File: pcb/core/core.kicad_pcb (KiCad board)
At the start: 2 copper layers, 24 x 26 mm, 25 parts, among them J1 Conn_01x10, J2 Conn_01x07, J3 Conn_ARM_SWD_TagConnect_TC203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, J4 Conn_01x10, U1 bq25185, U2 MDBT50-512K, U3 MCP1662-xOT

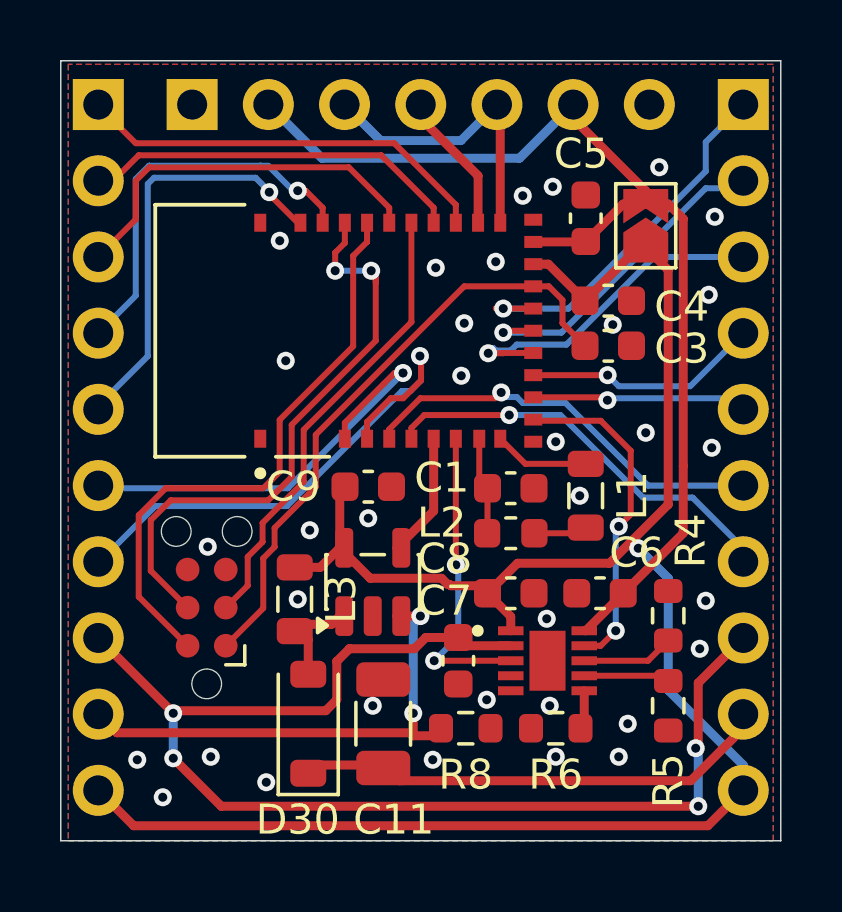
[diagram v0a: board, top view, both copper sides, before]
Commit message: Some fixes on PCB
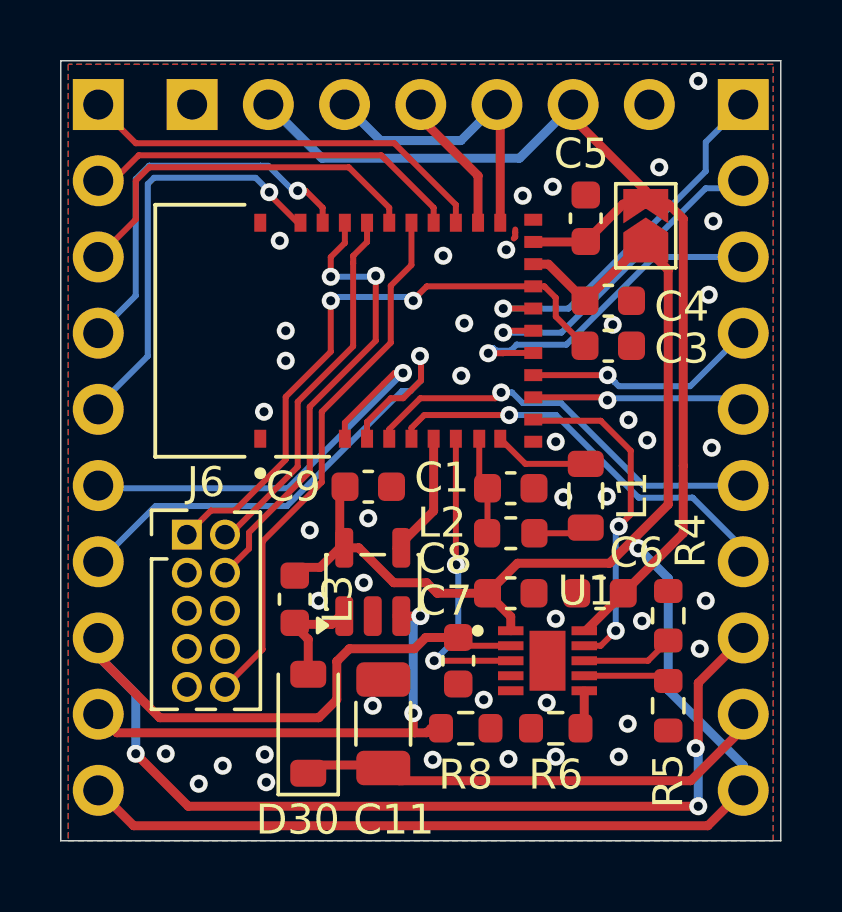
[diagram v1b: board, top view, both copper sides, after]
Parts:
- removed J3: Conn_ARM_SWD_TagConnect_TC2030-NL, Connector:Tag-Connect_TC2030-IDC-NL_2x03_P1.27mm_Vertical
- added J6: Conn_02x05_Odd_Even, Connector_PinHeader_1.27mm:PinHeader_2x05_P1.27mm_Vertical, F.Cu at (76.7, 92.3)
- L3: footprint Inductor_SMD:L_0805_2012Metric -> Inductor_SMD:L_0603_1608Metric
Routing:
- net /SWDIO: track 19.8 -> 12.5 mm
- net +BATT: track 42.6 -> 47.3 mm, vias 4 -> 3
- net /SWCLK: track 19.9 -> 15.7 mm
- net /RESET: track 15.4 -> 18.0 mm
- net GND: track 0.00 -> 0.32 mm, vias 34 -> 42
- net VDD: track 20.6 -> 20.3 mm, vias 0 -> 2
